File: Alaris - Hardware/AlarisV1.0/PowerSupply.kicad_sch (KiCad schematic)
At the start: 20 parts, among them U6 AMS1117-3.3, U7 AMS1117-1.8

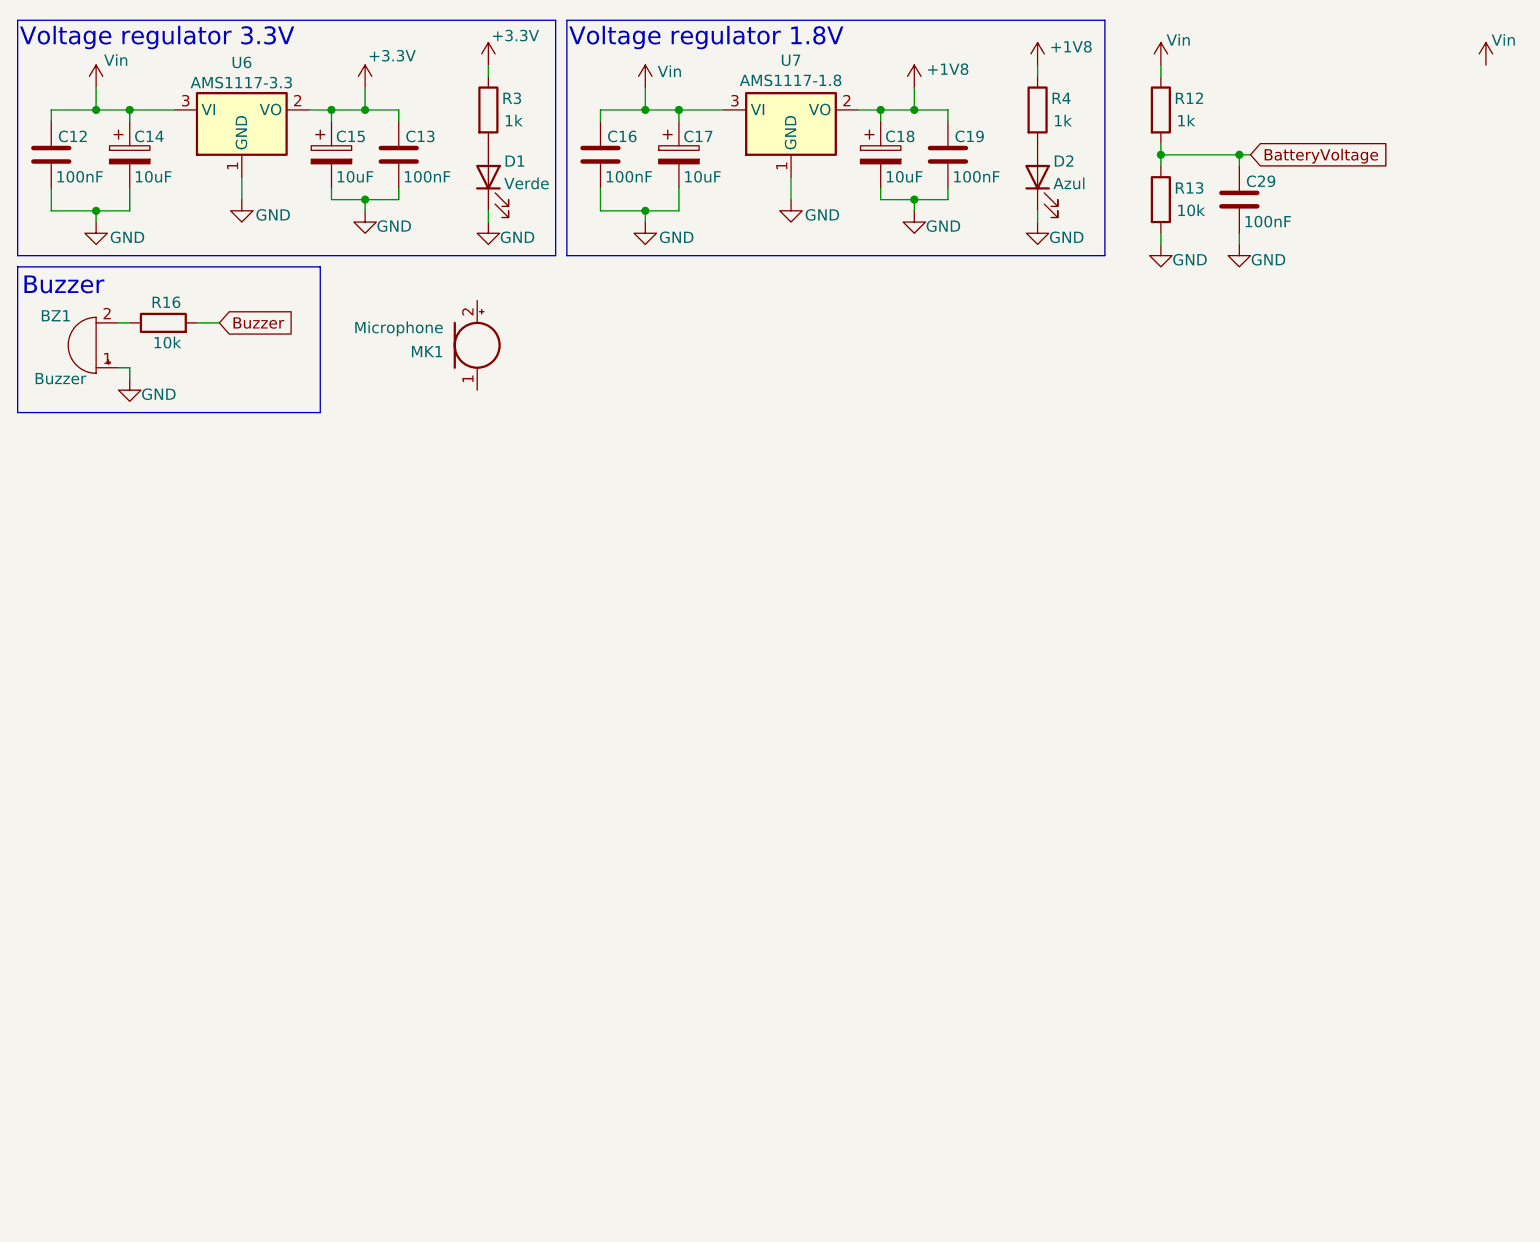
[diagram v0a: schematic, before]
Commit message: Desenvolvimento do Hardware
Desenvolvido os modulos de DAPN, GNCN, LDIN

Ainda é necessario implementação de alguns sensores, e melhor o modulo de gerenciamento de energia da placa
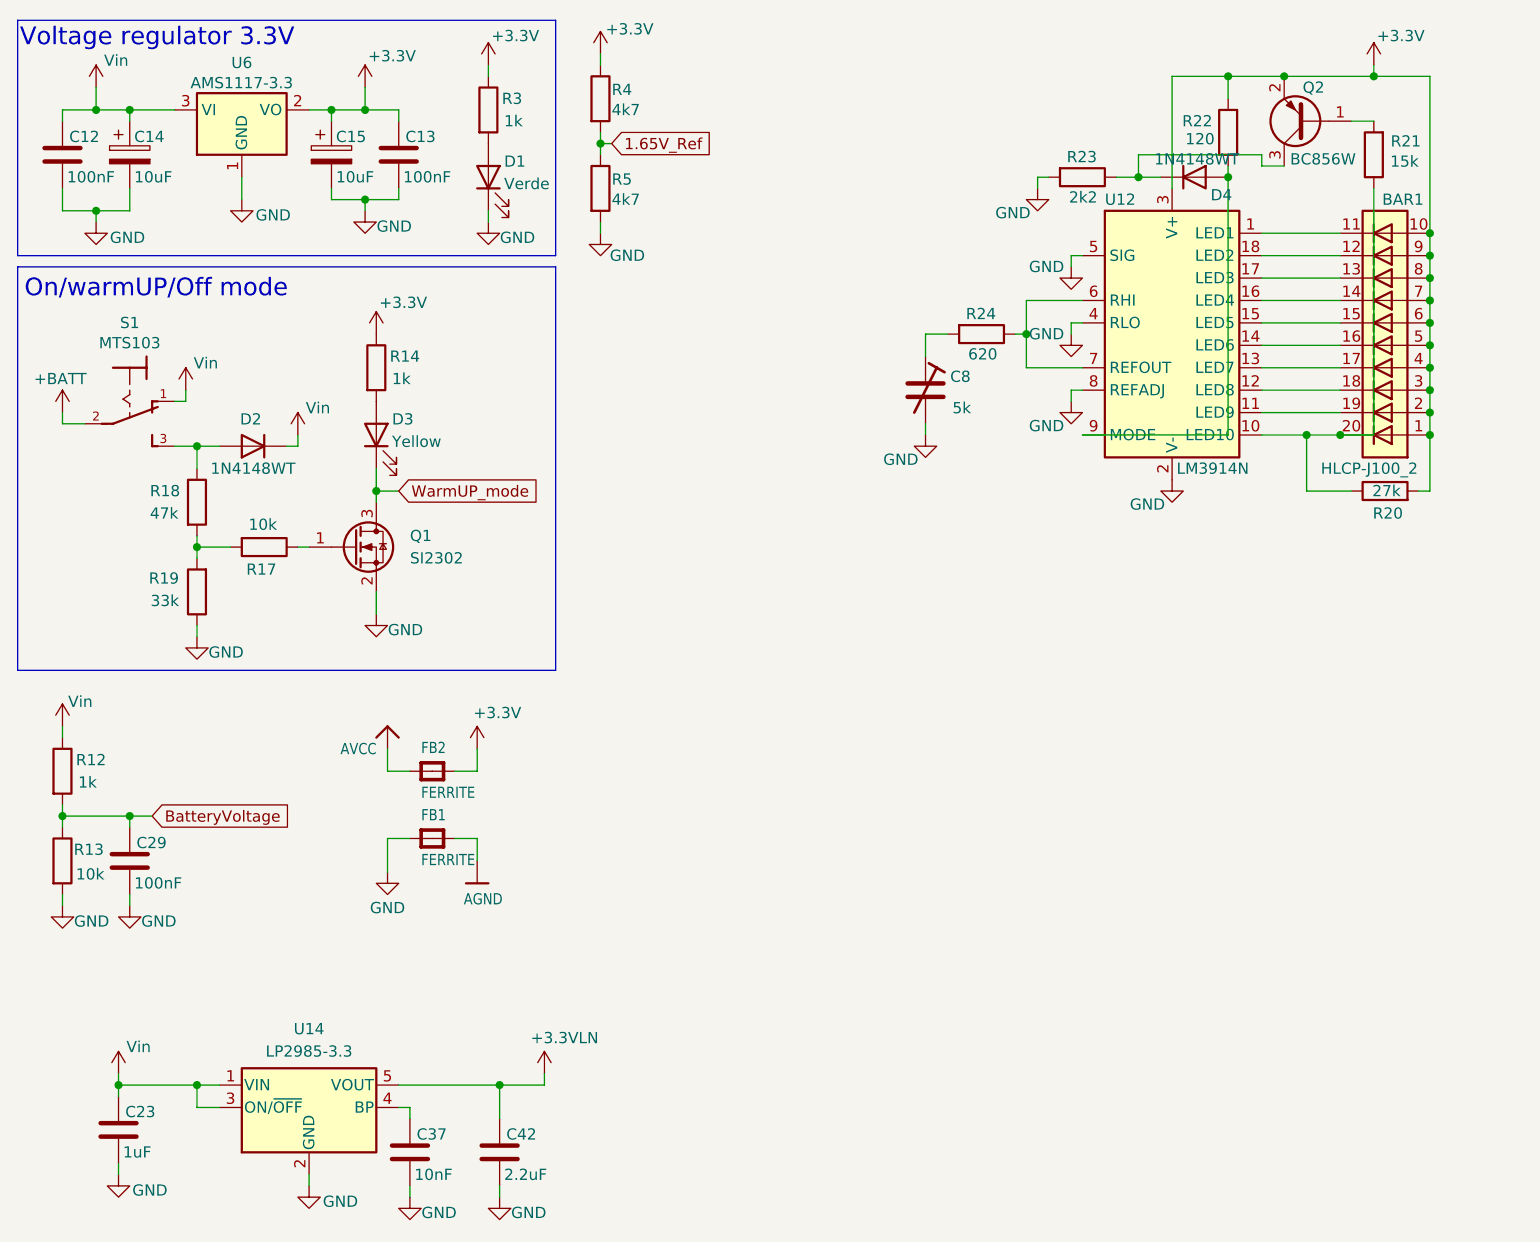
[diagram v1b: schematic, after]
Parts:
- removed BZ1: Buzzer, symbol Device:Buzzer
- removed C16, C19: 100nF, symbol Device:C
- removed C17, C18: 10uF, symbol Device:C_Polarized
- removed D2: Azul, symbol Device:LED
- removed MK1: Microphone, symbol Device:Microphone
- removed R16: 10k, symbol Device:R
- removed U7: AMS1117-1.8, Package_TO_SOT_SMD:SOT-223-3_TabPin2, symbol Regulator_Linear:AMS1117-1.8
- added BAR1: HLCP-J100_2, Display:HLCP-J100, symbol LED:HLCP-J100_2
- added C23: 1uF, Capacitor_SMD:C_0603_1608Metric_Pad1.08x0.95mm_HandSolder, symbol Device:C
- added C37: 10nF, Capacitor_SMD:C_0603_1608Metric_Pad1.08x0.95mm_HandSolder, symbol Device:C
- added C42: 2.2uF, Capacitor_SMD:C_0603_1608Metric_Pad1.08x0.95mm_HandSolder, symbol Device:C
- added C8: 5k, symbol Device:C_Trim
- added D2, D4: 1N4148WT, Diode_SMD:D_SOD-523, symbol Diode:1N4148WT
- added D3: Yellow, LED_SMD:LED_0603_1608Metric_Pad1.05x0.95mm_HandSolder, symbol Device:LED
- added FB1, FB2: FERRITE, Adafruit MAX4466 Mic Amp:0805, symbol Adafruit MAX4466 Mic Amp-eagle-import:FERRITE0805
- added Q1: SI2302, symbol Transistor_FET:Q_NMOS_GSD
- added Q2: BC856W, Package_TO_SOT_SMD:SOT-323_SC-70, symbol Transistor_BJT:BC856W
- added R14: 1k, Resistor_SMD:R_0603_1608Metric_Pad0.98x0.95mm_HandSolder, symbol Device:R
- added R17: 10k, Resistor_SMD:R_0603_1608Metric_Pad0.98x0.95mm_HandSolder, symbol Device:R
- added R18: 47k, Resistor_SMD:R_0603_1608Metric_Pad0.98x0.95mm_HandSolder, symbol Device:R
- added R19: 33k, Resistor_SMD:R_0603_1608Metric_Pad0.98x0.95mm_HandSolder, symbol Device:R
- added R20: 27k, Resistor_SMD:R_0603_1608Metric_Pad0.98x0.95mm_HandSolder, symbol Device:R
- added R21: 15k, Resistor_SMD:R_0603_1608Metric_Pad0.98x0.95mm_HandSolder, symbol Device:R
- added R22: 120, Resistor_SMD:R_0603_1608Metric_Pad0.98x0.95mm_HandSolder, symbol Device:R
- added R23: 2k2, Resistor_SMD:R_0603_1608Metric_Pad0.98x0.95mm_HandSolder, symbol Device:R
- added R24: 620, Resistor_SMD:R_0603_1608Metric_Pad0.98x0.95mm_HandSolder, symbol Device:R
- added R5: 4k7, Resistor_SMD:R_0603_1608Metric_Pad0.98x0.95mm_HandSolder, symbol Device:R
- added S1: MTS103, Footprint:MTS103, symbol Switch MTS103:MTS103
- added U12: LM3914N, Package_DIP:DIP-18_W7.62mm, symbol Driver_LED:LM3914N
- added U14: LP2985-3.3, Package_TO_SOT_SMD:SOT-23-5, symbol Regulator_Linear:LP2985-3.3
- C12, C13, C29: footprint (none) -> Capacitor_SMD:C_0603_1608Metric_Pad1.08x0.95mm_HandSolder
- D1: footprint (none) -> LED_SMD:LED_0603_1608Metric_Pad1.05x0.95mm_HandSolder
- R12, R13: footprint (none) -> Resistor_SMD:R_0603_1608Metric_Pad0.98x0.95mm_HandSolder
- R3: footprint (none) -> Resistor_SMD:R_0201_0603Metric_Pad0.64x0.40mm_HandSolder
- R4: value 1k -> 4k7; footprint (none) -> Resistor_SMD:R_0603_1608Metric_Pad0.98x0.95mm_HandSolder
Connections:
- net +1V8 is gone; now on net +3.3V: R4.1
- net +3.3V: now also BAR1.1 (A), BAR1.10 (A), BAR1.2 (A), BAR1.3 (A), BAR1.4 (A), BAR1.5 (A), BAR1.6 (A), BAR1.7 (A), BAR1.8 (A), BAR1.9 (A), FB2.2 (P$2), Q2.2 (E), R14.1, R20.2, R22.2, U12.3 (V+)
- net GND: now also C23.2, C37.2, C42.2, C8.2, FB1.1 (P$1), Q1.2 (S), R19.1, R23.2, R5.2, U12.2 (V-), U12.4 (RLO), U12.5 (SIG), U12.8 (REFADJ), U14.2 (GND)
- net Vin: now also C23.1, D2.1 (K), S1.1, U14.1 (VIN), U14.3 (ON/~{OFF})
- net 1.65V_Ref: now reaches R4.2
- net 1.65V_Ref: now also R5.1
- new net: Q1.1 (G), R17.1
- new net: D3.2 (A), R14.2
- new net: R17.2, R18.2, R19.2
- new net: Q2.1 (B), R21.2
- new net: D4.1 (K), Q2.3 (C), R23.1
- new net: C37.1, U14.4 (BP)
- new net: BAR1.11 (K), U12.1 (LED1)
- new net: BAR1.20 (K), R20.1, R21.1, U12.10 (LED10)
- new net: BAR1.19 (K), U12.11 (LED9)
- new net: BAR1.18 (K), U12.12 (LED8)
- new net: BAR1.17 (K), U12.13 (LED7)
- new net: BAR1.16 (K), U12.14 (LED6)
- new net: BAR1.15 (K), U12.15 (LED5)
- new net: BAR1.14 (K), U12.16 (LED4)
- new net: BAR1.13 (K), U12.17 (LED3)
- new net: BAR1.12 (K), U12.18 (LED2)
- new net: R24.1, U12.6 (RHI), U12.7 (REFOUT)
- new net: D4.2 (A), R22.1, U12.9 (MODE)
- new net: D2.2 (A), R18.1, S1.3
- new net: C8.1, R24.2
- new net +3.3VLN: C42.1, U14.5 (VOUT)
- new net +BATT: S1.2
- new net AGND: FB1.2 (P$2)
- new net AVCC: FB2.1 (P$1)
- new net WarmUP_mode: D3.1 (K), Q1.3 (D)
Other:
- note added: "On/warmUP/Off mode"
- note removed: "Buzzer"
- note removed: "Voltage regulator 1.8V"
- moved on the sheet: C12, C29, R12, R13
